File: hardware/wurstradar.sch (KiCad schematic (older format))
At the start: 10 parts

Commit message: verified rx path schematic in ltspice, fixed some values
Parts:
- C? (x2): value C -> 1u
- R?: value 8800 -> 8k8
- R?: value 1200 -> 1k2
- R? (x2): value 10k -> 4k7
- Rf: value 350 -> 3k5
- Rg: value 100 -> 1k
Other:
- note added: "MCP6273T-E/CH"
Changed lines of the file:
@@
-EESchema Schematic File Version 3
+EESchema Schematic File Version 2
 LIBS:power
 LIBS:device
+LIBS:transistors
+LIBS:conn
 LIBS:linear
 LIBS:regul
+LIBS:74xx
+LIBS:cmos4000
 LIBS:adc-dac
 LIBS:memory
@@
 LIBS:digital-audio
 LIBS:philips
+LIBS:display
 LIBS:cypress
 LIBS:siliconi
@@
 LIBS:atmel
 LIBS:contrib
+LIBS:valves
 LIBS:wurstradar-cache
-EELAYER 26 0
+EELAYER 25 0
 EELAYER END
 $Descr A4 11693 8268
@@
 P 5100 3550
 F 0 "R?" H 5170 3596 50  0000 L CNN
-F 1 "8800" H 5170 3505 50  0000 L CNN
+F 1 "8k8" H 5170 3505 50  0000 L CNN
 F 2 "" V 5030 3550 50  0001 C CNN
 F 3 "" H 5100 3550 50  0001 C CNN
@@
 P 5100 4150
 F 0 "R?" H 5170 4196 50  0000 L CNN
-F 1 "1200" H 5170 4105 50  0000 L CNN
+F 1 "1k2" H 5170 4105 50  0000 L CNN
 F 2 "" V 5030 4150 50  0001 C CNN
 F 3 "" H 5100 4150 50  0001 C CNN
@@
 P 5700 4850
 F 0 "Rg" H 5770 4896 50  0000 L CNN
-F 1 "100" H 5770 4805 50  0000 L CNN
+F 1 "1k" H 5770 4805 50  0000 L CNN
 F 2 "" V 5630 4850 50  0001 C CNN
 F 3 "" H 5700 4850 50  0001 C CNN
@@
 P 6250 4650
 F 0 "Rf" V 6043 4650 50  0000 C CNN
-F 1 "350" V 6134 4650 50  0000 C CNN
+F 1 "3k5" V 6134 4650 50  0000 C CNN
 F 2 "" V 6180 4650 50  0001 C CNN
 F 3 "" H 6250 4650 50  0001 C CNN
@@
 P 7550 3650
 F 0 "R?" H 7620 3696 50  0000 L CNN
-F 1 "10k" H 7620 3605 50  0000 L CNN
+F 1 "4k7" H 7620 3605 50  0000 L CNN
 F 2 "" V 7480 3650 50  0001 C CNN
 F 3 "" H 7550 3650 50  0001 C CNN
@@
 P 7550 4250
 F 0 "R?" H 7620 4296 50  0000 L CNN
-F 1 "10k" H 7620 4205 50  0000 L CNN
+F 1 "4k7" H 7620 4205 50  0000 L CNN
 F 2 "" V 7480 4250 50  0001 C CNN
 F 3 "" H 7550 4250 50  0001 C CNN
@@
 P 4850 3850
 F 0 "C?" V 4598 3850 50  0000 C CNN
-F 1 "C" V 4689 3850 50  0000 C CNN
+F 1 "1u" V 4689 3850 50  0000 C CNN
 F 2 "" H 4888 3700 50  0001 C CNN
 F 3 "" H 4850 3850 50  0001 C CNN
@@
 P 7100 3950
 F 0 "C?" V 6848 3950 50  0000 C CNN
-F 1 "C" V 6939 3950 50  0000 C CNN
+F 1 "1u" V 6939 3950 50  0000 C CNN
 F 2 "" H 7138 3800 50  0001 C CNN
 F 3 "" H 7100 3950 50  0001 C CNN
@@
 Text Notes 7950 3700 1    60   ~ 0
 +300 — +3000mV
+Text Notes 6150 2800 1    60   ~ 0
+MCP6273T-E/CH
 $EndSCHEMATC

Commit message: hardware preps for pcb
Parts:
- removed AE?: Antenna, symbol Antenna
- removed C? (x2): 1u, symbol C
- removed R?: 8k8, symbol R
- removed R?: 1k2, symbol R
- removed R? (x2): 4k7, symbol R
- removed Rf: 3k5, symbol R
- removed Rg: 1k, symbol R
- removed U?: LM321, TO_SOT_Packages_SMD:SOT-23-5, symbol LM321
- added C? (x2): 10u, symbol C
- added C?: 47u, symbol C
- added J?: RSM2650, Pin_Headers:Pin_Header_Straight_1x05_Pitch2.54mm, symbol Conn_01x05
- added J?: PowerBrick, symbol Conn_01x03
- added J?: PWR, symbol Conn_01x02
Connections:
- net labels added: +5V, VCC
- net labels removed: +3.3V
- wire segments 17 -> 19
- no-connect marks 0 -> 1
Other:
- note removed: "+100 — +700mV"
- note removed: "+300 — +3000mV"
- note removed: "+450 — +3150mV"
- note removed: "-300 — +300mV"
- note removed: "Amplification:\n1+Rf/Rg\n= 4.5"
- note removed: "MCP6273T-E/CH"

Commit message: updated schematic to current
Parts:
- removed C?: 10u, symbol C
- removed C?: 47u, symbol C
- added C? (x2): 47u 16V, symbol CP
- added D?: 1N4148, symbol D
- added D?: 1N4001, symbol D
- added J?: analog display, symbol Conn_01x02
- added R?: 470, symbol R
- C?: value 10u -> 10u 50V
- J?: value PowerBrick -> TPSM84205
- J?: value PWR -> 7..28V power in
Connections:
- wire segments 19 -> 37
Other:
- note added: "N-chan mosfet\nLR3636"
- note added: "drain"
- note added: "gate"
- note added: "source"
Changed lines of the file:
@@
-EESchema Schematic File Version 2
+EESchema Schematic File Version 3
 LIBS:power
 LIBS:device
-LIBS:transistors
-LIBS:conn
 LIBS:linear
 LIBS:regul
-LIBS:74xx
-LIBS:cmos4000
 LIBS:adc-dac
 LIBS:memory
@@
 LIBS:digital-audio
 LIBS:philips
-LIBS:display
 LIBS:cypress
 LIBS:siliconi
@@
 LIBS:atmel
 LIBS:contrib
-LIBS:valves
 LIBS:atmel_local
 LIBS:irf
@@
 LIBS:toshiba
 LIBS:wurstradar-cache
-EELAYER 25 0
+EELAYER 26 0
 EELAYER END
 $Descr A4 11693 8268
@@
 P 1300 1850
 F 0 "J?" H 1300 2050 50  0000 C CNN
-F 1 "PowerBrick" H 1300 1650 50  0000 C CNN
+F 1 "TPSM84205" H 1300 1650 50  0000 C CNN
 F 2 "" H 1300 1850 50  0001 C CNN
 F 3 "" H 1300 1850 50  0001 C CNN
@@
 P 1300 1350
 F 0 "J?" H 1300 1450 50  0000 C CNN
-F 1 "PWR" H 1300 1150 50  0000 C CNN
+F 1 "7..28V power in" H 1300 1150 50  0000 C CNN
 F 2 "" H 1300 1350 50  0001 C CNN
 F 3 "" H 1300 1350 50  0001 C CNN
@@
 L VCC #PWR?
 U 1 1 5A8CF859
-P 1600 1250
-F 0 "#PWR?" H 1600 1100 50  0001 C CNN
-F 1 "VCC" H 1600 1400 50  0000 C CNN
-F 2 "" H 1600 1250 50  0001 C CNN
-F 3 "" H 1600 1250 50  0001 C CNN
-	1    1600 1250
-	0    1    1    0
-$EndComp
-Wire Wire Line
-	1600 1250 1500 1250
+P 2000 1250
+F 0 "#PWR?" H 2000 1100 50  0001 C CNN
+F 1 "VCC" H 2000 1400 50  0000 C CNN
+F 2 "" H 2000 1250 50  0001 C CNN
+F 3 "" H 2000 1250 50  0001 C CNN
+	1    2000 1250
+	0    1    1    0
+$EndComp
+Wire Wire Line
+	2000 1250 1900 1250
 Wire Wire Line
 	1500 1350 1800 1350
@@
 P 2450 1550
 F 0 "C?" H 2475 1650 50  0000 L CNN
-F 1 "10u" H 2475 1450 50  0000 L CNN
+F 1 "10u 50V" H 2475 1450 50  0000 L CNN
 F 2 "" H 2488 1400 50  0001 C CNN
 F 3 "" H 2450 1550 50  0001 C CNN
 	1    2450 1550
-	-1   0    0    1
-$EndComp
-$Comp
-L C C?
-U 1 1 5A8D0354
-P 3050 1550
-F 0 "C?" H 3075 1650 50  0000 L CNN
-F 1 "10u" H 3075 1450 50  0000 L CNN
-F 2 "" H 3088 1400 50  0001 C CNN
-F 3 "" H 3050 1550 50  0001 C CNN
-	1    3050 1550
-	-1   0    0    1
-$EndComp
-$Comp
-L C C?
-U 1 1 5A8D03CE
-P 2800 1550
-F 0 "C?" H 2825 1650 50  0000 L CNN
-F 1 "47u" H 2825 1450 50  0000 L CNN
-F 2 "" H 2838 1400 50  0001 C CNN
-F 3 "" H 2800 1550 50  0001 C CNN
-	1    2800 1550
-	-1   0    0    1
-$EndComp
-Wire Wire Line
-	3050 1400 3050 1300
-Wire Wire Line
-	3050 1300 2800 1300
-Wire Wire Line
-	2800 1200 2800 1400
-Wire Wire Line
-	2800 1700 2800 1900
-Wire Wire Line
-	2800 1800 3050 1800
-Wire Wire Line
-	3050 1800 3050 1700
+	1    0    0    -1
+$EndComp
+Wire Wire Line
+	3650 1300 3650 1400
+Wire Wire Line
+	3050 1300 3650 1300
+Wire Wire Line
+	3050 1800 3650 1800
+Wire Wire Line
+	3650 1800 3650 1700
 Wire Wire Line
 	2450 1400 2450 1200
@@
 L GND #PWR?
 U 1 1 5A8D1307
-P 2800 1900
-F 0 "#PWR?" H 2800 1650 50  0001 C CNN
-F 1 "GND" H 2800 1750 50  0000 C CNN
-F 2 "" H 2800 1900 50  0001 C CNN
-F 3 "" H 2800 1900 50  0001 C CNN
-	1    2800 1900
-	1    0    0    -1
-$EndComp
-Connection ~ 2800 1800
+P 3350 1900
+F 0 "#PWR?" H 3350 1650 50  0001 C CNN
+F 1 "GND" H 3350 1750 50  0000 C CNN
+F 2 "" H 3350 1900 50  0001 C CNN
+F 3 "" H 3350 1900 50  0001 C CNN
+	1    3350 1900
+	1    0    0    -1
+$EndComp
 $Comp
 L VCC #PWR?
@@
 L +5V #PWR?
 U 1 1 5A8D13FE
-P 2800 1200
-F 0 "#PWR?" H 2800 1050 50  0001 C CNN
-F 1 "+5V" H 2800 1340 50  0000 C CNN
-F 2 "" H 2800 1200 50  0001 C CNN
-F 3 "" H 2800 1200 50  0001 C CNN
-	1    2800 1200
-	1    0    0    -1
-$EndComp
-Connection ~ 2800 1300
+P 3350 1200
+F 0 "#PWR?" H 3350 1050 50  0001 C CNN
+F 1 "+5V" H 3350 1340 50  0000 C CNN
+F 2 "" H 3350 1200 50  0001 C CNN
+F 3 "" H 3350 1200 50  0001 C CNN
+	1    3350 1200
+	1    0    0    -1
+$EndComp
 Wire Wire Line
 	2850 4200 3250 4200
 Wire Wire Line
 	2850 4400 3250 4400
+$Comp
+L CP C?
+U 1 1 5A958A8B
+P 3050 1550
+F 0 "C?" H 3168 1596 50  0000 L CNN
+F 1 "47u 16V" H 3168 1505 50  0000 L CNN
+F 2 "" H 3088 1400 50  0001 C CNN
+F 3 "" H 3050 1550 50  0001 C CNN
+	1    3050 1550
+	1    0    0    -1
+$EndComp
+$Comp
+L CP C?
+U 1 1 5A958C31
+P 3650 1550
+F 0 "C?" H 3768 1596 50  0000 L CNN
+F 1 "47u 16V" H 3768 1505 50  0000 L CNN
+F 2 "" H 3688 1400 50  0001 C CNN
+F 3 "" H 3650 1550 50  0001 C CNN
+	1    3650 1550
+	1    0    0    -1
+$EndComp
+Wire Wire Line
+	3350 1900 3350 1800
+Connection ~ 3350 1800
+Wire Wire Line
+	3350 1300 3350 1200
+Connection ~ 3350 1300
+Wire Wire Line
+	3050 1300 3050 1400
+Wire Wire Line
+	3050 1800 3050 1700
+$Comp
+L R R?
+U 1 1 5A9596E6
+P 6250 4400
+F 0 "R?" V 6043 4400 50  0000 C CNN
+F 1 "470" V 6134 4400 50  0000 C CNN
+F 2 "" V 6180 4400 50  0001 C CNN
+F 3 "" H 6250 4400 50  0001 C CNN
+	1    6250 4400
+	0    1    1    0
+$EndComp
+$Comp
+L D D?
+U 1 1 5A959893
+P 6400 3400
+F 0 "D?" V 6354 3479 50  0000 L CNN
+F 1 "1N4148" V 6445 3479 50  0000 L CNN
+F 2 "" H 6400 3400 50  0001 C CNN
+F 3 "" H 6400 3400 50  0001 C CNN
+	1    6400 3400
+	0    1    1    0
+$EndComp
+$Comp
+L Conn_01x02 J?
+U 1 1 5A959B56
+P 7300 3350
+F 0 "J?" H 7220 3025 50  0000 C CNN
+F 1 "analog display" H 7220 3116 50  0000 C CNN
+F 2 "" H 7300 3350 50  0001 C CNN
+F 3 "" H 7300 3350 50  0001 C CNN
+	1    7300 3350
+	1    0    0    -1
+$EndComp
+Wire Wire Line
+	6800 3150 6800 3350
+Wire Wire Line
+	6400 3150 6800 3150
+Wire Wire Line
+	6400 3150 6400 3250
+Wire Wire Line
+	6800 3650 6800 3450
+Wire Wire Line
+	6400 3650 6800 3650
+Wire Wire Line
+	6400 3650 6400 3550
+$Comp
+L +5V #PWR?
+U 1 1 5A959E88
+P 6600 3050
+F 0 "#PWR?" H 6600 2900 50  0001 C CNN
+F 1 "+5V" H 6615 3223 50  0000 C CNN
+F 2 "" H 6600 3050 50  0001 C CNN
+F 3 "" H 6600 3050 50  0001 C CNN
+	1    6600 3050
+	1    0    0    -1
+$EndComp
+Wire Wire Line
+	6600 3050 6600 3150
+Connection ~ 6600 3150
+Wire Wire Line
+	6600 3650 6600 3900
+Connection ~ 6600 3650
+$Comp
+L GND #PWR?
+U 1 1 5A959FE0
+P 6600 4500
+F 0 "#PWR?" H 6600 4250 50  0001 C CNN
+F 1 "GND" H 6605 4327 50  0000 C CNN
+F 2 "" H 6600 4500 50  0001 C CNN
+F 3 "" H 6600 4500 50  0001 C CNN
+	1    6600 4500
+	1    0    0    -1
+$EndComp
+Wire Wire Line
+	6600 4300 6600 4500
+Wire Wire Line
+	6600 4400 6400 4400
+Connection ~ 6600 4400
+Wire Wire Line
+	5450 4400 6100 4400
+Wire Wire Line
+	6000 4400 6000 4050
+Wire Wire Line
+	6000 4050 6200 4050
+Connection ~ 6000 4400
+Text Notes 6600 4400 0    60   ~ 0
+source
+Text Notes 6600 3900 0    60   ~ 0
+drain
+Text Notes 6000 4050 0    60   ~ 0
+gate
+Text Notes 6350 4150 0    60   ~ 0
+N-chan mosfet\nLR3636
+Wire Notes Line
+	6200 3900 6200 4300
+Wire Notes Line
+	6200 4300 7300 4300
+Wire Notes Line
+	7300 4300 7300 3900
+Wire Notes Line
+	7300 3900 6200 3900
+$Comp
+L D D?
+U 1 1 5A95B437
+P 1750 1250
+F 0 "D?" H 1750 1466 50  0000 C CNN
+F 1 "1N4001" H 1750 1375 50  0000 C CNN
+F 2 "" H 1750 1250 50  0001 C CNN
+F 3 "" H 1750 1250 50  0001 C CNN
+	1    1750 1250
+	1    0    0    -1
+$EndComp
+Wire Wire Line
+	1600 1250 1500 1250
+Wire Wire Line
+	6800 3450 7100 3450
+Wire Wire Line
+	6800 3350 7100 3350
 $EndSCHEMATC

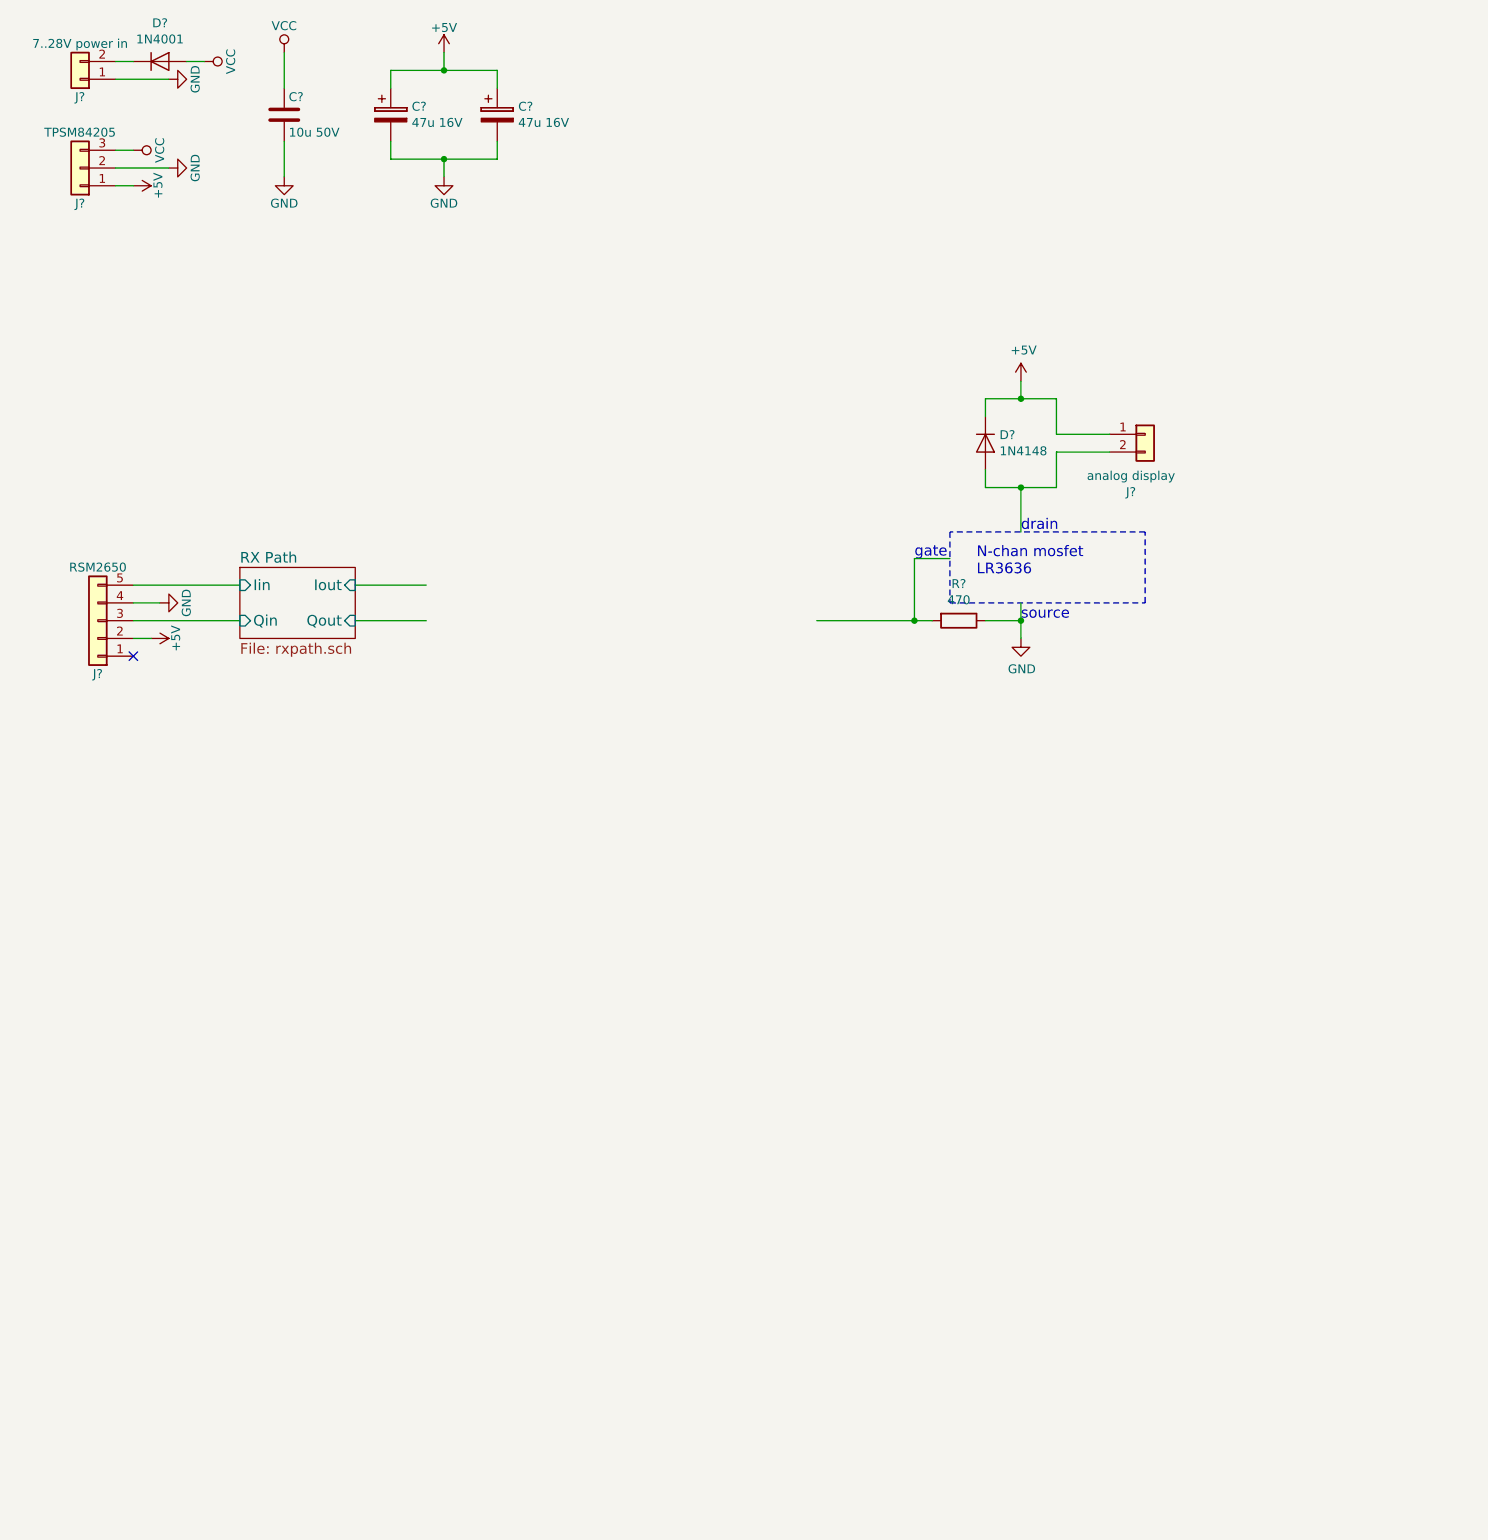
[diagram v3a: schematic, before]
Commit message: integrate FFT library (dunno if it works...)
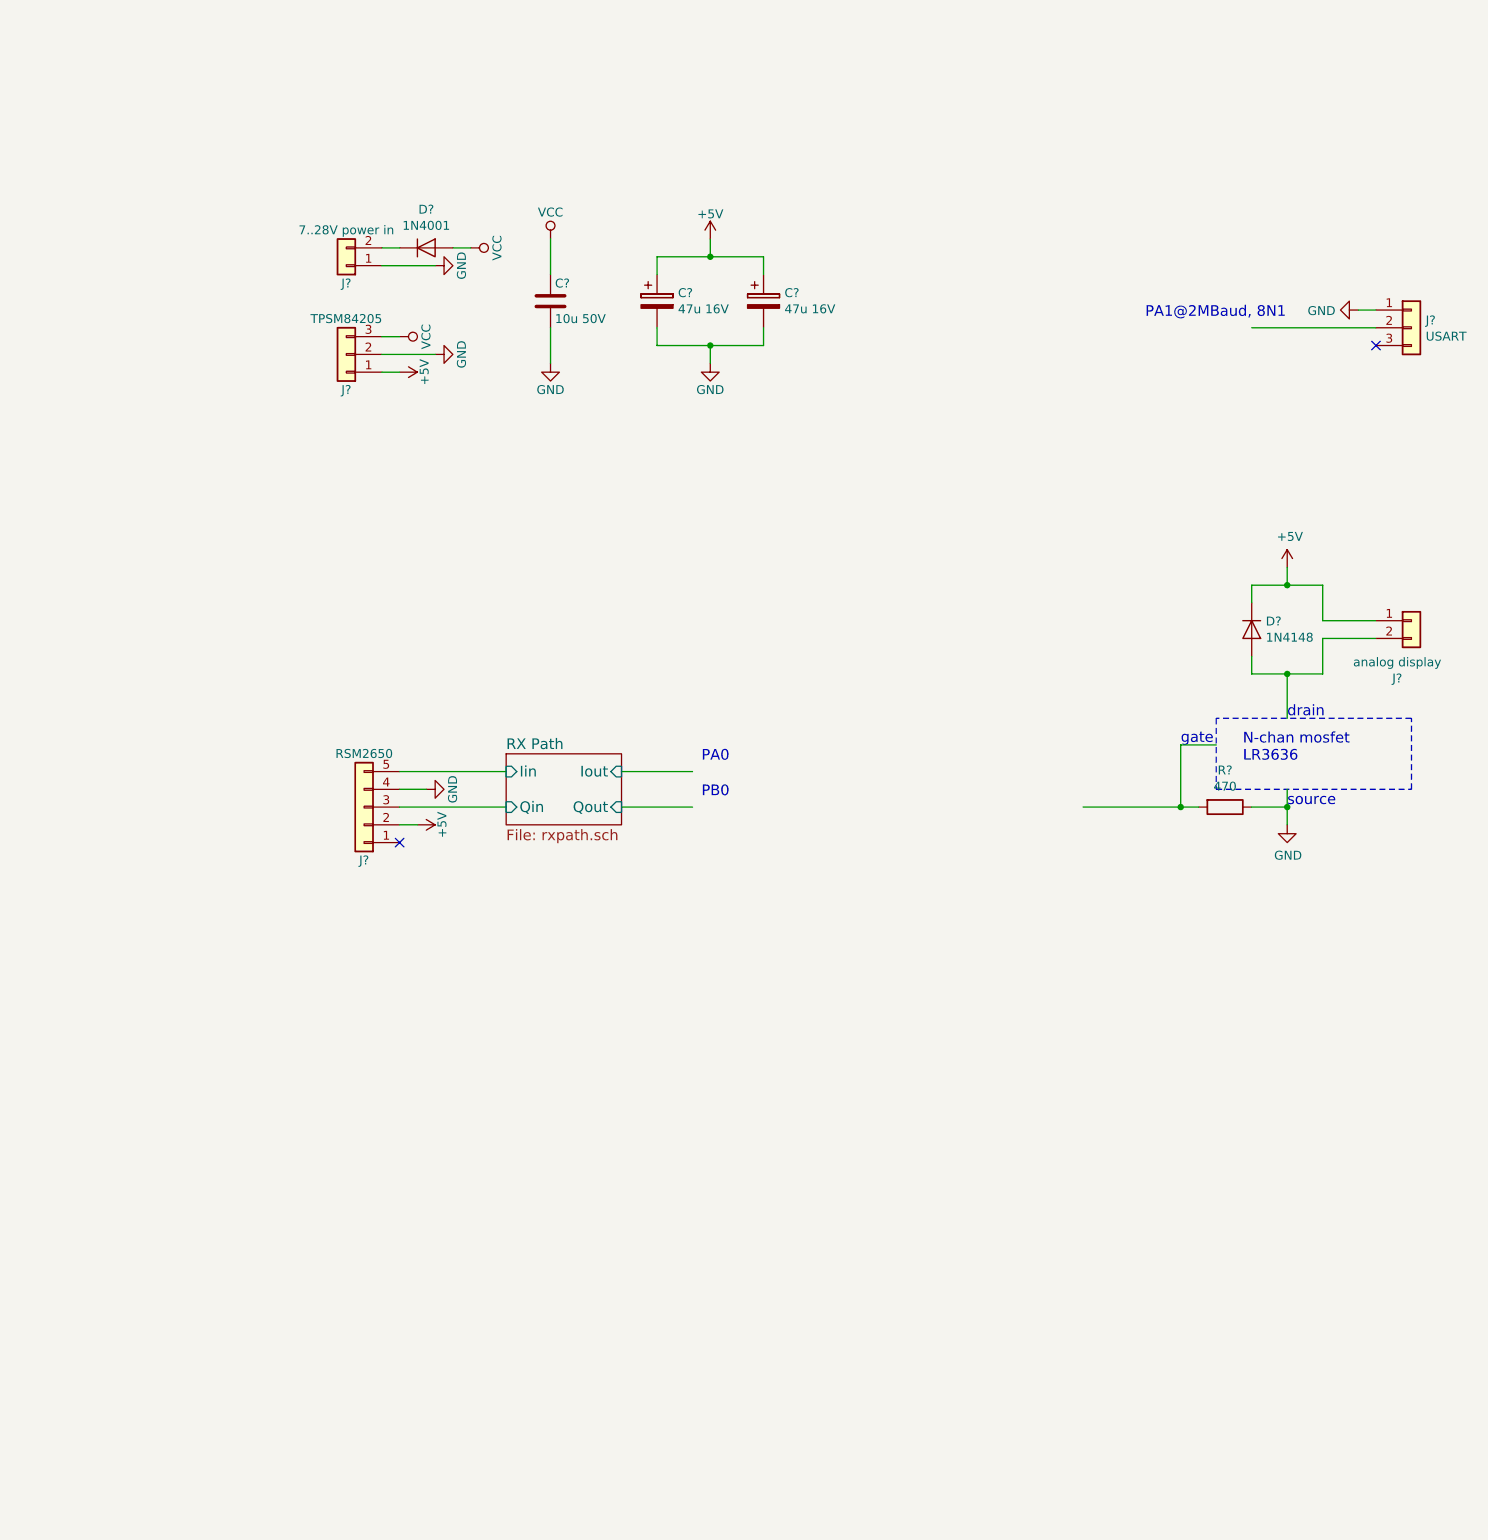
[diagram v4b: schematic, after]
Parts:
- added J?: USART, symbol Conn_01x03
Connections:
- wire segments 37 -> 39
- no-connect marks 1 -> 2
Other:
- note added: "PA0"
- note added: "PA1@2MBaud, 8N1"
- note added: "PB0"
- moved on the sheet: C?, D?, J?, R?
